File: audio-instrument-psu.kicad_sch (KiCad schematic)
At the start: 27 parts, among them J1 Conn_01x04_Male, J2 Conn_01x04_Male, J3 Conn_01x04_Male, J4 Conn_01x04_Male, J99 Mini-DIN-4, U1 LM317_TO-220, U2 LM337_TO220

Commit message: Working on TODO list
- add mounting holes/brackets
- add LED connector
- add switch connector
- add license/kicad decals
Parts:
- removed J1, J2, J3, J4: Conn_01x04_Male, Connector_Molex_KK-396:Molex_KK-396_A-41791-0004_1x04_P3.96mm_Vertical, symbol Connector:Conn_01x04_Male
- added H1, H2: MountingHole_Pad, Mounting_gkeeth:MountingBracket_Keystone_4335_Width12.7mm_Drill3.05mm, symbol Mechanical:MountingHole_Pad
- added H3, H4: MountingHole_Pad, MountingHole:MountingHole_3.2mm_M3_Pad, symbol Mechanical:MountingHole_Pad
- added J1, J2, J3, J4, J6: Molex_SL_01x04_Male, Connector_Molex_SL:Molex_SL_A-70543-0003_1x04_P2.54mm_Vertical, symbol Connector_gkeeth:Molex_SL_01x04_Male
- added J5: Molex_SL_01x02_Male, Connector_Molex_SL:Molex_SL_A-70543-0001_1x02_P2.54mm_Vertical, symbol Connector_gkeeth:Molex_SL_01x02_Male
- added LOGO?: CC-BY-SA_0.33in, Symbol_CreativeCommons:CC-BY-SA_SilkScreenTop_Small, symbol Creative_Commons:CC-BY-SA_0.33in
- added LOGO?: Logo_MadeWithKiCad, Symbol:KiCad-Logo2_5mm_SilkScreen, symbol Graphic_gkeeth:Logo_MadeWithKiCad
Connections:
- net +12V: now also J2.1 (Pin_1), J3.1 (Pin_1), J4.1 (Pin_1), J6.1 (Pin_1)
- net -12V: now also J2.4 (Pin_4), J3.4 (Pin_4), J4.4 (Pin_4), J6.4 (Pin_4)
- net GND: now also H1.1, H2.1, H3.1, H4.1, J1.3 (Pin_3), J1.4 (Pin_4), J2.2 (Pin_2), J2.3 (Pin_3), J3.2 (Pin_2), J3.3 (Pin_3), J4.2 (Pin_2), J4.3 (Pin_3), J6.2 (Pin_2), J6.3 (Pin_3)
- net at D1.2 (A), D2.1 (K): now also J5.2 (Pin_2)
- new net: J1.1 (Pin_1), J1.2 (Pin_2), J5.1 (Pin_1)
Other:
- note added: "TODO: - check mirroring on mini-din connector"
- note added: "to on/off switch"
- note added: "to power LEDs"
- note removed: "TODO: - check mirroring on mini-din connector - mounting holes - mounting brackets - CC-BY-SA, made with kicad"

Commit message: add to TODO list
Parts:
- added R5, R6: 10k, Resistor_SMD:R_1206_3216Metric, symbol Device:R
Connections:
- net +12V: now also R5.1; no longer J6.1 (Pin_1)
- net -12V: now also R6.1; no longer J6.4 (Pin_4)
- new net: J6.4 (Pin_4), R6.2
- new net: J6.1 (Pin_1), R5.2
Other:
- note added: "TODO: - check mirroring on mini-din connector - snubber? - DPDT power switch? - test points? check against preamp power supply"
- note removed: "TODO: - check mirroring on mini-din connector"
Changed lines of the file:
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@@
+    (stroke (width 0) (type default) (color 0 0 0 0))
+  )
+  (wire (pts (xy 326.39 199.39) (xy 327.66 199.39))
     (stroke (width 0) (type default) (color 0 0 0 0))
   )
@@
     (stroke (width 0) (type default) (color 0 0 0 0))
   )
-  (wire (pts (xy 328.93 201.93) (xy 335.28 201.93))
+  (wire (pts (xy 321.31 201.93) (xy 335.28 201.93))
     (stroke (width 0) (type default) (color 0 0 0 0))
   )
@@
     (stroke (width 0) (type default) (color 0 0 0 0))
   )
+  (wire (pts (xy 326.39 207.01) (xy 326.39 212.09))
+    (stroke (width 0) (type default) (color 0 0 0 0))
+  )
   (wire (pts (xy 242.57 134.62) (xy 242.57 135.89))
     (stroke (width 0) (type default) (color 0 0 0 0))
@@
     (stroke (width 0) (type default) (color 0 0 0 0))
   )
-  (wire (pts (xy 335.28 196.85) (xy 335.28 199.39))
+  (wire (pts (xy 326.39 195.58) (xy 326.39 199.39))
     (stroke (width 0) (type default) (color 0 0 0 0))
   )
@@
     (stroke (width 0) (type default) (color 0 0 0 0))
   )
-  (wire (pts (xy 328.93 207.01) (xy 328.93 201.93))
+  (wire (pts (xy 321.31 203.2) (xy 321.31 201.93))
     (stroke (width 0) (type default) (color 0 0 0 0))
   )
@@
     (stroke (width 0) (type default) (color 0 0 0 0))
   )
+  (wire (pts (xy 326.39 207.01) (xy 327.66 207.01))
+    (stroke (width 0) (type default) (color 0 0 0 0))
+  )
   (wire (pts (xy 228.6 157.48) (xy 228.6 160.02))
     (stroke (width 0) (type default) (color 0 0 0 0))
@@
   )
   (wire (pts (xy 242.57 147.32) (xy 228.6 147.32))
-    (stroke (width 0) (type default) (color 0 0 0 0))
-  )
-  (wire (pts (xy 335.28 209.55) (xy 335.28 207.01))
     (stroke (width 0) (type default) (color 0 0 0 0))
   )
@@
     (effects (font (size 1.27 1.27)) (justify left bottom))
   )
-  (text "TODO:\n- check mirroring on mini-din connector" (at 25.4 259.08 0)
+  (text "TODO:\n- check mirroring on mini-din connector\n- snubber?\n- DPDT power switch?\n- test points?\n\ncheck against preamp power supply"
+    (at 25.4 259.08 0)
     (effects (font (size 1.27 1.27)) (justify left bottom))
   )
@@
     (pin "1")
   )
+  (symbol (lib_id "Device:R") (at 331.47 207.01 90) (unit 1)
+    (in_bom yes) (on_board yes) (fields_autoplaced)
+    (property "Reference" "R6" (id 0) (at 331.47 210.82 90))
+    (property "Value" "10k" (id 1) (at 331.47 213.36 90))
+    (property "Footprint" "Resistor_SMD:R_1206_3216Metric" (id 2) (at 331.47 208.788 90)
+      (effects (font (size 1.27 1.27)) hide)
+    )
+    (property "Datasheet" "~" (id 3) (at 331.47 207.01 0)
+      (effects (font (size 1.27 1.27)) hide)
+    )
+    (pin "1")
+    (pin "2")
+  )
   (symbol (lib_id "Device:R") (at 242.57 153.67 0) (unit 1)
     (in_bom yes) (on_board yes) (fields_autoplaced)
@@
     (pin "2")
   )
+  (symbol (lib_id "Device:R") (at 331.47 199.39 90) (unit 1)
+    (in_bom yes) (on_board yes) (fields_autoplaced)
+    (property "Reference" "R5" (id 0) (at 331.47 193.04 90))
+    (property "Value" "10k" (id 1) (at 331.47 195.58 90))
+    (property "Footprint" "Resistor_SMD:R_1206_3216Metric" (id 2) (at 331.47 201.168 90)
+      (effects (font (size 1.27 1.27)) hide)
+    )
+    (property "Datasheet" "~" (id 3) (at 331.47 199.39 0)
+      (effects (font (size 1.27 1.27)) hide)
+    )
+    (pin "1")
+    (pin "2")
+  )
   (symbol (lib_id "power:GND") (at 198.12 248.92 0) (unit 1)
     (in_bom yes) (on_board yes) (fields_autoplaced)
@@
     (pin "1")
   )
-  (symbol (lib_id "power:GND") (at 328.93 207.01 0) (unit 1)
-    (in_bom yes) (on_board yes) (fields_autoplaced)
-    (property "Reference" "#PWR?" (id 0) (at 328.93 213.36 0)
-      (effects (font (size 1.27 1.27)) hide)
-    )
-    (property "Value" "GND" (id 1) (at 328.93 212.09 0))
-    (property "Footprint" "" (id 2) (at 328.93 207.01 0)
-      (effects (font (size 1.27 1.27)) hide)
-    )
-    (property "Datasheet" "" (id 3) (at 328.93 207.01 0)
+  (symbol (lib_id "power:GND") (at 321.31 203.2 0) (unit 1)
+    (in_bom yes) (on_board yes) (fields_autoplaced)
+    (property "Reference" "#PWR?" (id 0) (at 321.31 209.55 0)
+      (effects (font (size 1.27 1.27)) hide)
+    )
+    (property "Value" "GND" (id 1) (at 321.31 208.28 0))
+    (property "Footprint" "" (id 2) (at 321.31 203.2 0)
+      (effects (font (size 1.27 1.27)) hide)
+    )
+    (property "Datasheet" "" (id 3) (at 321.31 203.2 0)
       (effects (font (size 1.27 1.27)) hide)
     )
@@
     (pin "1")
   )
-  (symbol (lib_id "power:-12V") (at 335.28 209.55 0) (mirror x) (unit 1)
-    (in_bom yes) (on_board yes) (fields_autoplaced)
-    (property "Reference" "#PWR?" (id 0) (at 335.28 212.09 0)
-      (effects (font (size 1.27 1.27)) hide)
-    )
-    (property "Value" "-12V" (id 1) (at 335.28 214.63 0))
-    (property "Footprint" "" (id 2) (at 335.28 209.55 0)
-      (effects (font (size 1.27 1.27)) hide)
-    )
-    (property "Datasheet" "" (id 3) (at 335.28 209.55 0)
+  (symbol (lib_id "power:-12V") (at 326.39 212.09 0) (mirror x) (unit 1)
+    (in_bom yes) (on_board yes) (fields_autoplaced)
+    (property "Reference" "#PWR?" (id 0) (at 326.39 214.63 0)
+      (effects (font (size 1.27 1.27)) hide)
+    )
+    (property "Value" "-12V" (id 1) (at 326.39 217.17 0))
+    (property "Footprint" "" (id 2) (at 326.39 212.09 0)
+      (effects (font (size 1.27 1.27)) hide)
+    )
+    (property "Datasheet" "" (id 3) (at 326.39 212.09 0)
       (effects (font (size 1.27 1.27)) hide)
     )
@@
     (pin "2")
   )
-  (symbol (lib_id "power:+12V") (at 335.28 196.85 0) (unit 1)
-    (in_bom yes) (on_board yes) (fields_autoplaced)
-    (property "Reference" "#PWR?" (id 0) (at 335.28 200.66 0)
-      (effects (font (size 1.27 1.27)) hide)
-    )
-    (property "Value" "+12V" (id 1) (at 335.28 191.77 0))
-    (property "Footprint" "" (id 2) (at 335.28 196.85 0)
-      (effects (font (size 1.27 1.27)) hide)
-    )
-    (property "Datasheet" "" (id 3) (at 335.28 196.85 0)
+  (symbol (lib_id "power:+12V") (at 326.39 195.58 0) (unit 1)
+    (in_bom yes) (on_board yes) (fields_autoplaced)
+    (property "Reference" "#PWR?" (id 0) (at 326.39 199.39 0)
+      (effects (font (size 1.27 1.27)) hide)
+    )
+    (property "Value" "+12V" (id 1) (at 326.39 190.5 0))
+    (property "Footprint" "" (id 2) (at 326.39 195.58 0)
+      (effects (font (size 1.27 1.27)) hide)
+    )
+    (property "Datasheet" "" (id 3) (at 326.39 195.58 0)
       (effects (font (size 1.27 1.27)) hide)
     )
@@
       (reference "R4") (unit 1) (value "270") (footprint "Resistor_SMD:R_1206_3216Metric")
     )
+    (path "/6f243e90-af38-45e8-a82c-310b21660da0"
+      (reference "R5") (unit 1) (value "10k") (footprint "Resistor_SMD:R_1206_3216Metric")
+    )
+    (path "/2fdd2555-b4cc-4324-92a4-015b84745f97"
+      (reference "R6") (unit 1) (value "10k") (footprint "Resistor_SMD:R_1206_3216Metric")
+    )
     (path "/99c92dc5-15e7-4980-aa06-c95c338d054c"

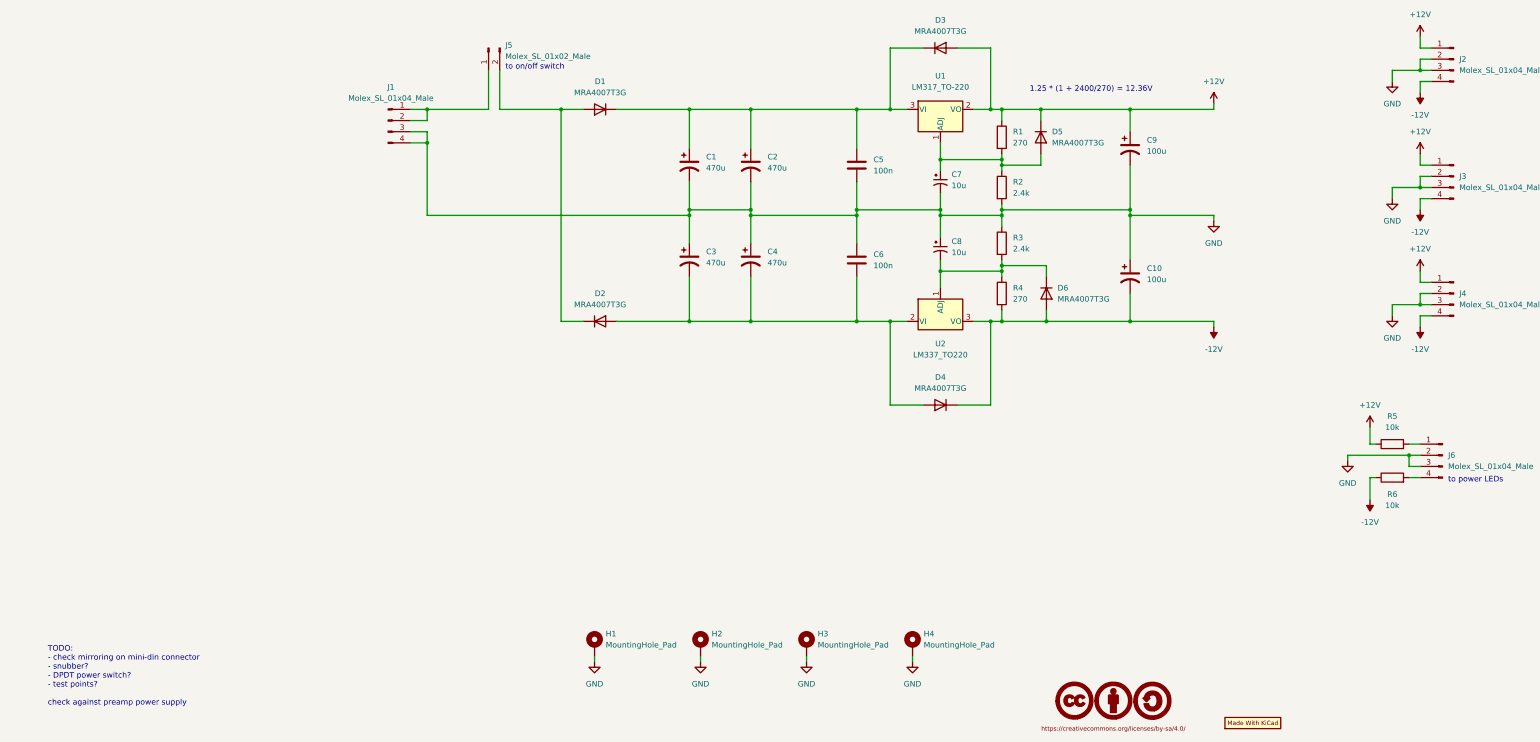
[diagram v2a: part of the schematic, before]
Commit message: Work through TODO list
- add testpoints
- simplify power switch connectors (wire directly from power connector
  to power switch, then power switch to board connector)
- add caps on ADJ pins
- add snubber
- ERC clean
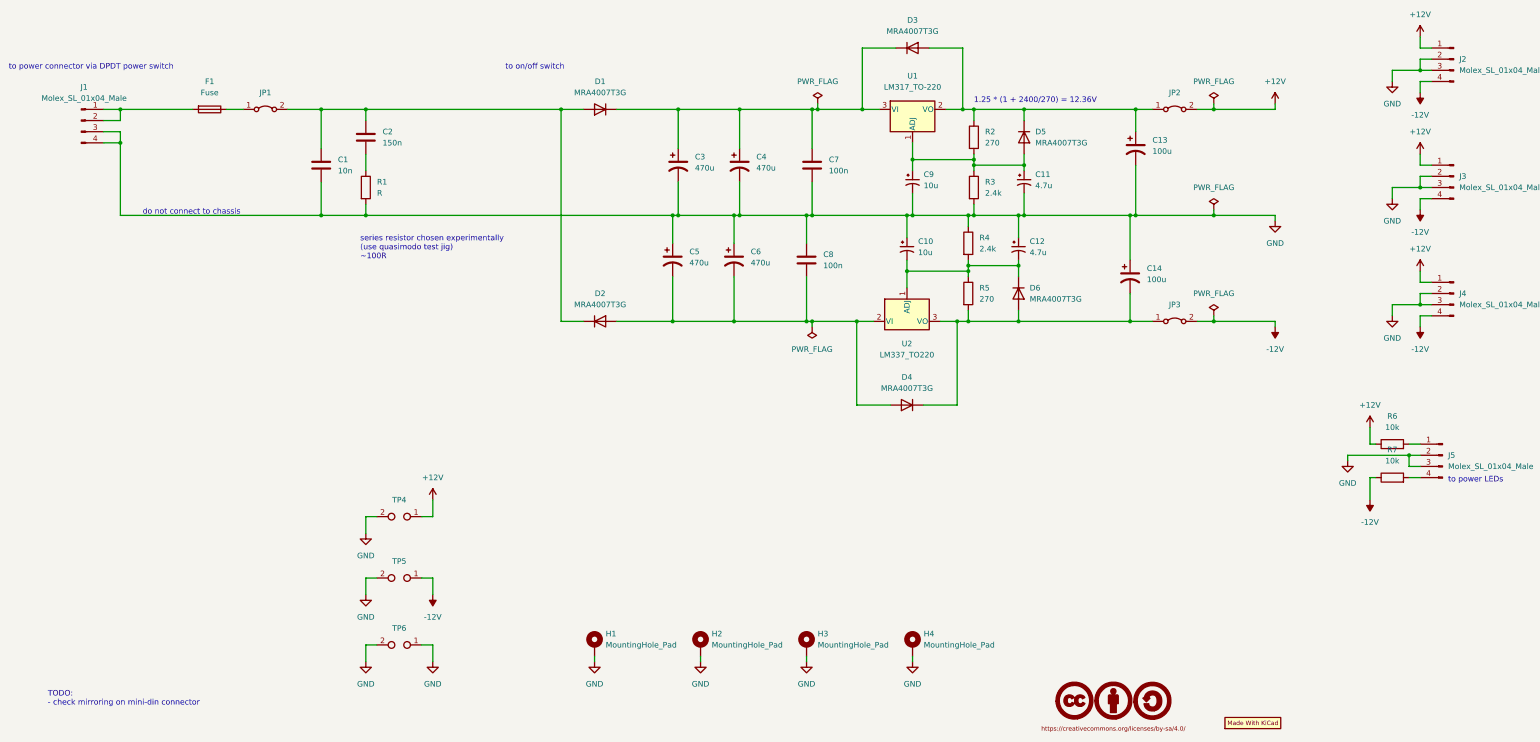
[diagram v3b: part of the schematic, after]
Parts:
- removed J5: Molex_SL_01x02_Male, Connector_Molex_SL:Molex_SL_A-70543-0001_1x02_P2.54mm_Vertical, symbol Connector_gkeeth:Molex_SL_01x02_Male
- added C1: 10n, Capacitor_THT:C_Rect_L7.2mm_W2.5mm_P5.00mm_FKS2_FKP2_MKS2_MKP2, symbol Device:C
- added C11, C12: 4.7u, Capacitor_THT:CP_Radial_D5.0mm_P2.00mm, symbol Device:C_Polarized_Small_US
- added C2: 150n, Capacitor_THT:C_Rect_L7.5mm_W6.5mm_P5.00mm, symbol Device:C
- added F1: Fuse, Fuse:Fuseholder_Cylinder-5x20mm_Schurter_0031_8201_Horizontal_Open, symbol Device:Fuse
- added JP1, JP2, JP3: Jumper_2_Bridged, Connector_PinHeader_2.54mm:PinHeader_1x02_P2.54mm_Vertical, symbol Jumper:Jumper_2_Bridged
- added R1: R, Resistor_SMD:R_1206_3216Metric, symbol Device:R
- added TP4, TP5, TP6: TestPoint_2Pole, Connector_PinHeader_2.54mm:PinHeader_1x02_P2.54mm_Vertical, symbol Connector:TestPoint_2Pole
- gave numbers to parts that had none: 2
- renumbered C8 to C10, C9 to C13, C10 to C14, C1 to C3, C2 to C4, C3 to C5, C4 to C6, C5 to C7, C6 to C8, C7 to C9, J6 to J5, R1 to R2, R2 to R3, R3 to R4, R4 to R5, R5 to R6, R6 to R7
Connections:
- net +12V: now also JP2.2 (B), TP4.1; no longer C13.1, D3.2 (A), D5.1 (K), R2.1, U1.2 (VO)
- net -12V: now also JP3.2 (B), TP5.1; no longer C14.2, D4.1 (K), D6.2 (A), R5.2, U2.3 (VO)
- net GND: now also C1.2, C11.2, C12.1, R1.2, TP4.2, TP5.2, TP6.1, TP6.2
- net at C9.1, D5.2 (A), R2.2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: now also C11.1
- net at D1.2 (A), D2.1 (K): now also C1.1, C2.1, JP1.2 (B)
- net at C10.2, D6.1 (K), R4.2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: now also C12.2
- net at J1.1 (Pin_1), J1.2 (Pin_2): now also F1.2
- new net: C2.2, R1.1
- new net: C13.1, D3.2 (A), D5.1 (K), JP2.1 (A), R2.1, U1.2 (VO)
- new net: C14.2, D4.1 (K), D6.2 (A), JP3.1 (A), R5.2, U2.3 (VO)
- new net: F1.1, JP1.1 (A)
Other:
- note added: "TODO: - check mirroring on mini-din connector"
- note added: "do not connect to chassis"
- note added: "series resistor chosen experimentally (use quasimodo test jig) ~100R"
- note added: "to power connector via DPDT power switch"
- note removed: "TODO: - check mirroring on mini-din connector - snubber? - DPDT power switch? - test points? check against preamp power supply"
- moved on the sheet: C10, C13, C3, C4, C5, C6, C7, C8, C9, D3, D4, D5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
